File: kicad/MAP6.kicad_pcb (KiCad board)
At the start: 2 copper layers, 49.9 x 74.9 mm, 35 parts, among them M1 Motor_vibration, P1 Logo_MA, P2 Pin, P3 LEG, P4 LEG, P5 LEG, P6 LEG, P7 LEG, P8 LEG, P9 STING, Q1 BC547, SW1 On, U1 LM555

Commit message: M19O2 MAP6 added .STEP CAD file
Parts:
- removed kibuzzard-611CDB3A: G***, label
- added kibuzzard-611CF906: G***, label, B.Cu at (131.6, 115.8)

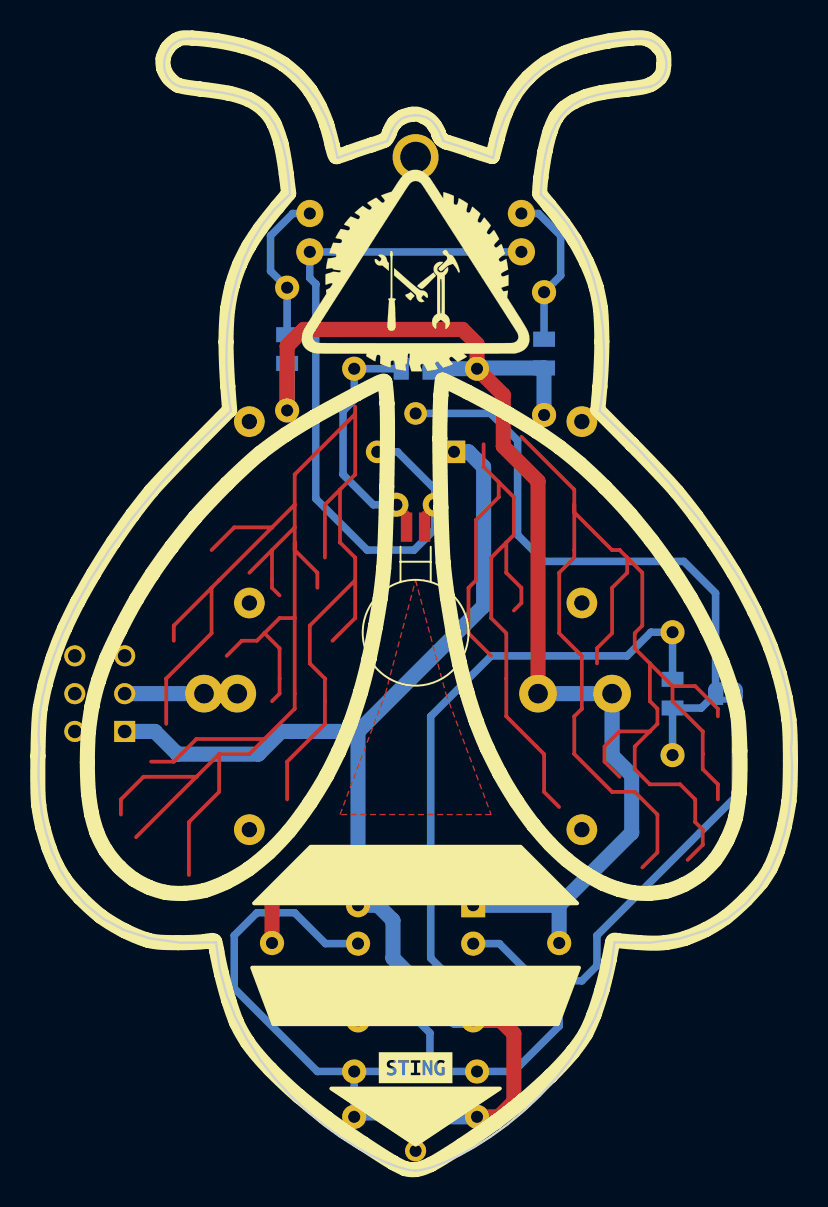
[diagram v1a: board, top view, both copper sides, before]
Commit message: M19O2 MAP6 cleaned SILK legend
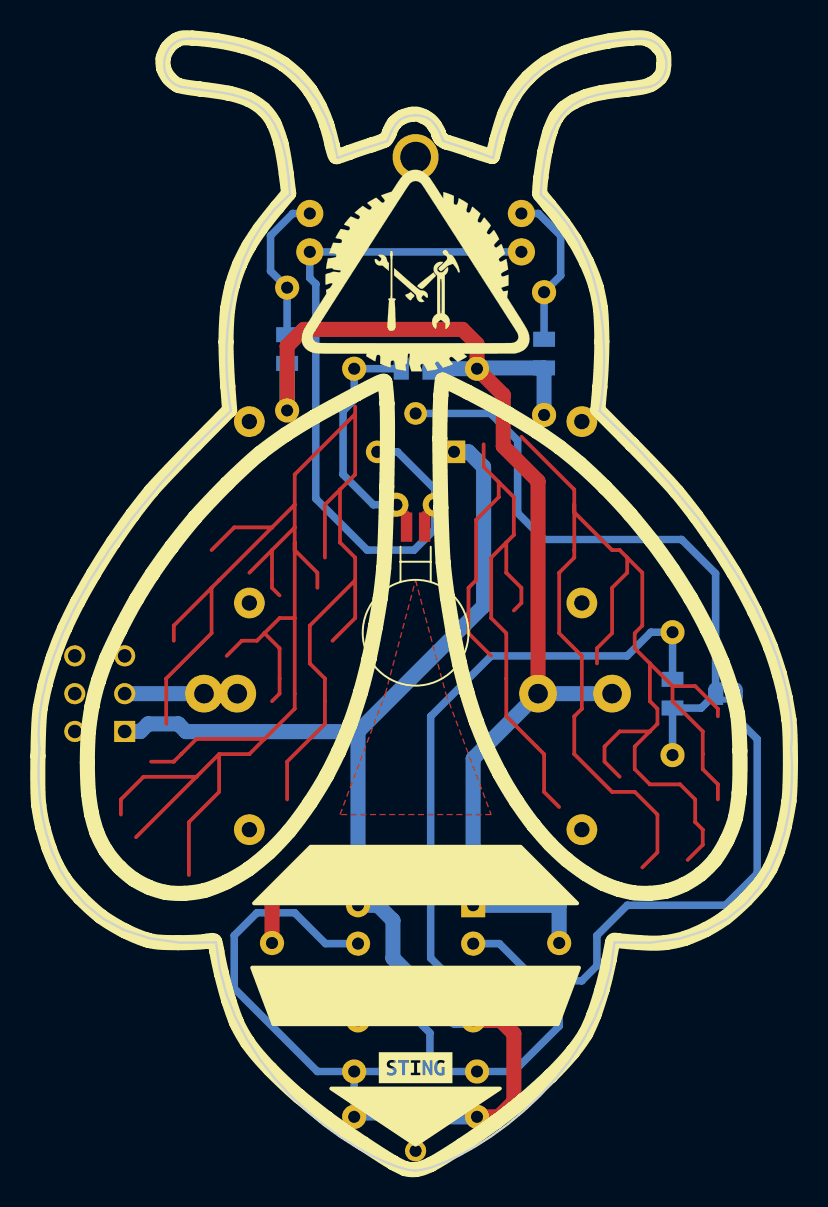
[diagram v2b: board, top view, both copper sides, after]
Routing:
- net Net-(C1-Pad1): track 52.9 -> 57.9 mm
- net /6V: track 77.3 -> 76.4 mm
- net /GND: track 390.1 -> 389.3 mm

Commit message: MAP6 Blender renders and amimations
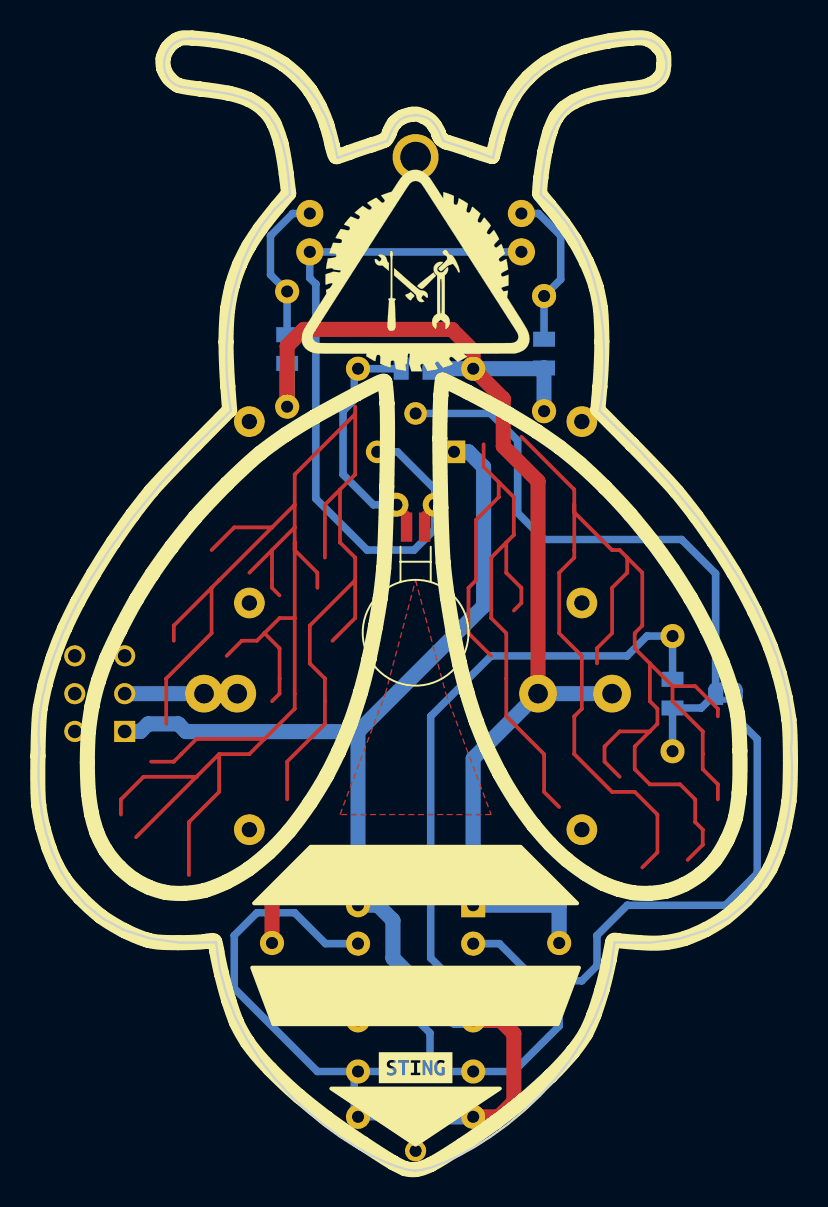
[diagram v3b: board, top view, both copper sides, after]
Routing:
- net /GND: track 389.3 -> 388.2 mm

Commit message: added interactive HTML BoM in /bom folder
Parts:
- R1, R2: value 10E -> 470E
- R3: value 10E -> 100E
- renumbered P1 to G1, LOGO1 to G10, P2 to G2, P3 to G3, P4 to G4, P5 to G5, P6 to G6, P7 to G7, P8 to G8, P9 to G9
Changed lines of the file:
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@@
   )
   (layers
-    (0 F.Cu signal hide)
-    (31 B.Cu signal hide)
-    (34 B.Paste user hide)
-    (35 F.Paste user hide)
+    (0 F.Cu signal)
+    (31 B.Cu signal)
+    (34 B.Paste user)
+    (35 F.Paste user)
     (36 B.SilkS user)
-    (37 F.SilkS user hide)
-    (38 B.Mask user hide)
-    (39 F.Mask user hide)
-    (40 Dwgs.User user hide)
+    (37 F.SilkS user)
+    (38 B.Mask user)
+    (39 F.Mask user)
+    (40 Dwgs.User user)
     (44 Edge.Cuts user)
-    (45 Margin user hide)
-    (46 B.CrtYd user hide)
-    (47 F.CrtYd user hide)
-    (48 B.Fab user hide)
-    (49 F.Fab user hide)
+    (45 Margin user)
+    (46 B.CrtYd user)
+    (47 F.CrtYd user)
+    (48 B.Fab user)
+    (49 F.Fab user)
   )
   (setup
@@
       (effects (font (size 0.9 0.9) (thickness 0.15)) (justify mirror))
     )
-    (fp_text value 10E (at 0 -1.714501 90) (layer B.SilkS) hide
+    (fp_text value 470E (at 0 -1.714501 90) (layer B.SilkS) hide
       (effects (font (size 0.9 0.9) (thickness 0.15)) (justify mirror))
     )
@@
       (effects (font (size 0.9 0.9) (thickness 0.15)) (justify mirror))
     )
-    (fp_text value 10E (at 0 -1.714501 90) (layer B.SilkS) hide
+    (fp_text value 470E (at 0 -1.714501 90) (layer B.SilkS) hide
       (effects (font (size 0.9 0.9) (thickness 0.15)) (justify mirror))
     )
@@
       (effects (font (size 0.9 0.9) (thickness 0.15)) (justify mirror))
     )
-    (fp_text value 10E (at 0 -1.7145) (layer B.SilkS) hide
+    (fp_text value 100E (at 0 -1.7145) (layer B.SilkS) hide
       (effects (font (size 0.9 0.9) (thickness 0.15)) (justify mirror))
     )
@@
     (at 167.75 118 180)
     (descr "Open Hardware Logo, 6x6mm")
-    (fp_text reference LOGO1 (at 0 0 180) (layer B.SilkS) hide
+    (fp_text reference G10 (at 0 0 180) (layer B.SilkS) hide
       (effects (font (size 0.9 0.9) (thickness 0.15)) (justify mirror))
     )
@@
   (module map6_fp:MTG_2mm (layer F.Cu)
     (at 148.5 75.5)
-    (fp_text reference P2 (at 0 1.27) (layer F.SilkS) hide
+    (fp_text reference G2 (at 0 1.27) (layer F.SilkS) hide
       (effects (font (size 0.9 0.9) (thickness 0.15)))
     )
@@
   (module map6_fp:MTG_1mm (layer B.Cu)
     (at 137.5 120)
-    (fp_text reference P3 (at 0 -1.27) (layer B.SilkS) hide
+    (fp_text reference G3 (at 0 -1.27) (layer B.SilkS) hide
       (effects (font (size 1 1) (thickness 0.15)) (justify mirror))
     )
@@
   (module map6_fp:MTG_1mm (layer B.Cu)
     (at 137.5 93)
-    (fp_text reference P4 (at 0 -1.27) (layer B.SilkS) hide
+    (fp_text reference G4 (at 0 -1.27) (layer B.SilkS) hide
       (effects (font (size 1 1) (thickness 0.15)) (justify mirror))
     )
@@
   (module map6_fp:MTG_1mm (layer B.Cu)
     (at 159.5 120)
-    (fp_text reference P5 (at 0 -1.27) (layer B.SilkS) hide
+    (fp_text reference G5 (at 0 -1.27) (layer B.SilkS) hide
       (effects (font (size 1 1) (thickness 0.15)) (justify mirror))
     )
@@
   (module map6_fp:MTG_1mm (layer B.Cu)
     (at 159.5 93)
-    (fp_text reference P6 (at 0 -1.27) (layer B.SilkS) hide
+    (fp_text reference G6 (at 0 -1.27) (layer B.SilkS) hide
       (effects (font (size 1 1) (thickness 0.15)) (justify mirror))
     )
@@
   (module map6_fp:MTG_1mm (layer B.Cu)
     (at 137.5 105)
-    (fp_text reference P7 (at 0 -1.27) (layer B.SilkS) hide
+    (fp_text reference G7 (at 0 -1.27) (layer B.SilkS) hide
       (effects (font (size 1 1) (thickness 0.15)) (justify mirror))
     )
@@
   (module map6_fp:MTG_1mm (layer B.Cu)
     (at 159.5 105)
-    (fp_text reference P8 (at 0 -1.27) (layer B.SilkS) hide
+    (fp_text reference G8 (at 0 -1.27) (layer B.SilkS) hide
       (effects (font (size 1 1) (thickness 0.15)) (justify mirror))
     )
@@
   (module map6_fp:MA_LOGO (layer F.Cu)
     (at 148.5 83)
-    (fp_text reference P1 (at 0 -2.25) (layer F.SilkS) hide
+    (fp_text reference G1 (at 0 -2.25) (layer F.SilkS) hide
       (effects (font (size 1.524 1.524) (thickness 0.3)))
     )
@@
   (module map6_fp:MTG_0mm8 (layer F.Cu)
     (at 148.5 141.25)
-    (fp_text reference P9 (at 0 1.27) (layer F.SilkS) hide
+    (fp_text reference G9 (at 0 1.27) (layer F.SilkS) hide
       (effects (font (size 1 1) (thickness 0.15)))
     )

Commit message: updated schematic and pcb
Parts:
- added kibuzzard-612E1065: G***, label, F.Cu at (148.5, 111.0)
- R1, R2: value 470E -> 150E
- R3: value 100E -> 15E
- R4, R6: footprint map6_fp:r_0805 -> map6_fp:r_0805_DNP
- kibuzzard-611CD92E: footprint label -> map6_fp:label_website
- kibuzzard-611CDC95 (x6): footprint label -> map6_fp:label_LEG
- kibuzzard-611CE09C: footprint label -> map6_fp:label_sting
- kibuzzard-611CF906: footprint label -> map6_fp:label_URL
- moved R3 5.00 mm to (148.5, 84.5)
- moved Q1 3.00 mm to (148.5, 92.0)
- moved M1 2.50 mm to (148.5, 102.5)
- moved R2 0.50 mm to (157.0, 88.0)
- moved kibuzzard-611CF906 0.40 mm to (132.0, 115.8)
- moved SW1 0.25 mm to (129.5, 113.5)
- moved R1 0.20 mm to (140.0, 88.0)
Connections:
- M1 pad 1: Net-(D1-Pad1) -> Net-(JP1-Pad2)
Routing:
- net /GND: track 388.2 -> 423.1 mm
- net Net-(D1-Pad1): track 49.6 -> 32.0 mm
- net Net-(JP1-Pad2): track 41.1 -> 52.0 mm
- net /motor: track 16.3 -> 19.5 mm
- net /6V: track 76.4 -> 78.6 mm
- net /right_eye: track 10.5 -> 10.0 mm
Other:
- rule pad_to_mask_clearance: 0.2 -> 0

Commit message: big update, added several battery options
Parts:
- added BT2: BAT, map6_fp:cr2032_04_3025-2, B.Cu at (146.9, 111.5)
- BT1: footprint map6_fp:cr2032_02 -> map6_fp:cr2032_03
- M1: value Motor_vibration -> Motor
- R1, R2: value 150E -> 220E
- R3: value 15E -> 47E
- R4: value DNP -> 1k; footprint map6_fp:r_0805_DNP -> map6_fp:r_0805
- R6: value DNP -> 10k; footprint map6_fp:r_0805_DNP -> map6_fp:r_0805
- SW1: footprint map6_fp:SW_CuK_JS202011AQN_DPDT_Angled -> map6_fp:SW_SPDT_Straight
- moved kibuzzard-611CD92E 30.0 mm to (148.5, 96.5)
- moved R5 29.0 mm to (148.5, 87.5), turned to 180 degrees
- moved kibuzzard-611CF906 27.7 mm to (148.5, 93.5), turned to 180 degrees
- moved R4 14.1 mm to (138.5, 129.0), turned to 90 degrees
- moved M1 12.5 mm to (148.5, 90.0)
- moved C2 10.5 mm to (147.2, 136.5), turned to 0 degrees
- moved kibuzzard-611CDC95 10.3 mm to (130.5, 110.0)
- moved kibuzzard-611CDC95 10.3 mm to (166.5, 110.0)
- moved R6 8.90 mm to (141.5, 130.5), turned to 90 degrees
- moved Q1 8.00 mm to (148.5, 84.0)
- moved kibuzzard-611CDC95 7.25 mm to (132.5, 123.0)
- moved kibuzzard-611CDC95 7.25 mm to (164.5, 123.0)
- moved JP1 6.50 mm to (171.5, 117.0), turned to 90 degrees
- moved G7 6.40 mm to (133.5, 110.0)
- moved G8 6.40 mm to (163.5, 110.0)
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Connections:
- M1 pad 1: Net-(JP1-Pad2) -> Net-(D1-Pad1)
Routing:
- net (no net): track 0.00 -> 385.3 mm
- net /GND: track 423.1 -> 126.5 mm
- net Net-(R5-Pad2): track 40.5 -> 67.4 mm
- net Net-(BT1-Pad1): track 7.20 -> 32.2 mm
- net Net-(R4-Pad1): track 32.3 -> 12.4 mm
- net /6V: track 78.6 -> 90.9 mm
- net Net-(C1-Pad1): track 57.9 -> 51.4 mm
- net Net-(D1-Pad1): track 32.0 -> 29.1 mm
- net /right_eye: track 10.0 -> 8.58 mm
- net /left_eye: track 10.0 -> 8.58 mm
- net Net-(JP1-Pad2): track 52.0 -> 53.5 mm
- net Net-(C2-Pad1): track 6.78 -> 5.67 mm

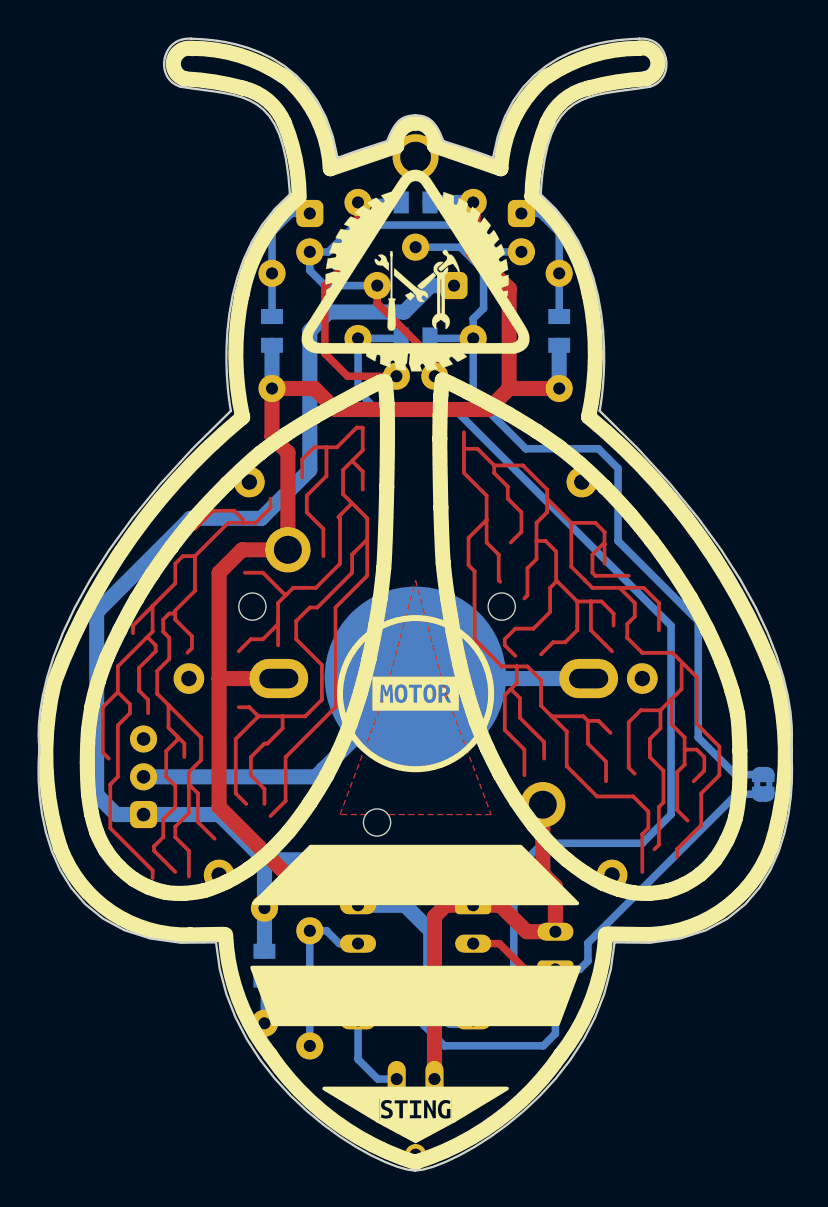
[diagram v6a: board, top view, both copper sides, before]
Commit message: another big update after deciding battery options. Ready for FAB
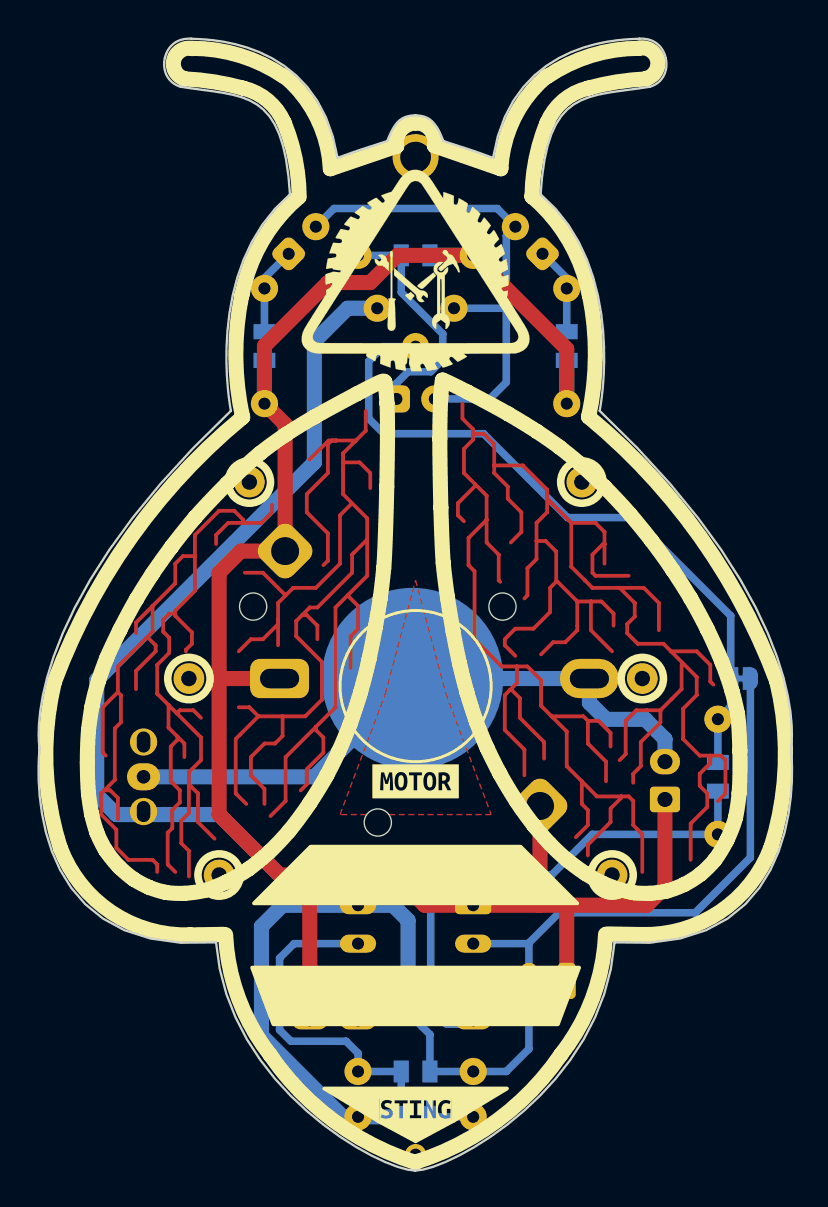
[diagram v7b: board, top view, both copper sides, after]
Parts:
- added J1: JST2, map6_fp:JST_EH_B2B-EH-A_1x02_P2.50mm_Vertical, B.Cu at (165.0, 118.0)
- moved R5 35.2 mm to (168.5, 116.5), turned to 270 degrees
- moved R1 19.5 mm to (158.5, 88.0)
- moved R2 19.5 mm to (138.5, 88.0)
- moved D1 14.5 mm to (156.0, 81.0), turned to 315 degrees
- moved D2 14.5 mm to (141.0, 81.0), turned to 225 degrees
- moved R4 14.1 mm to (148.5, 139.0), turned to 180 degrees
- moved G10 13.7 mm to (162.6, 101.1)
- moved R6 8.90 mm to (148.5, 136.0), turned to 180 degrees
- moved JP1 7.16 mm to (170.0, 110.0), turned to 180 degrees
- moved C2 6.94 mm to (141.5, 132.6), turned to 90 degrees
- moved kibuzzard-612E1065 5.80 mm to (148.5, 116.8)
- moved R3 3.50 mm to (148.5, 82.0)
- moved BT2 2.05 mm to (148.3, 110.0)
- moved C1 1.90 mm to (156.0, 130.0), turned to 0 degrees
- moved BT1 1.50 mm to (146.0, 110.0)
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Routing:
- net Net-(R5-Pad2): track 67.4 -> 31.8 mm
- net (no net): track 385.3 -> 408.4 mm
- net Net-(R4-Pad1): track 12.4 -> 27.6 mm
- net Net-(BT1-Pad1): track 32.2 -> 41.3 mm
- net /GND: track 126.5 -> 133.3 mm
- net Net-(JP1-Pad2): track 53.5 -> 46.7 mm
- net /6V: track 90.9 -> 96.2 mm
- net Net-(D1-Pad1): track 29.1 -> 33.4 mm
- net Net-(C1-Pad1): track 51.4 -> 55.4 mm
- net /motor: track 19.1 -> 15.6 mm
- net /right_eye: track 8.58 -> 5.82 mm
- net /left_eye: track 8.58 -> 5.82 mm
- net Net-(C2-Pad1): track 5.67 -> 3.19 mm
